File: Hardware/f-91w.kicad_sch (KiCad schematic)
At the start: 1 part, among them U2 LCD-F-91W

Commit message: Update Schematic and Add PIC and BME280 symbols
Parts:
- added C1: 4.7u, Capacitors_SMD:C_0402, symbol C
- added C2, C3: 22p, Capacitors_SMD:C_0402, symbol C
- added P1, P10, P11, P13, P14, P15, P2, P3, P4, P5, P6, P7, P8, P9: CONN_01X01, Connect:1pin, symbol Connector_Generic:Conn_01x01
- added Q1: BC846, Package_TO_SOT_SMD:SOT-23, symbol Transistor_BJT:BC846
- added R1: 10k, Resistors_SMD:R_0402, symbol R
- added R2: 47k, Resistors_SMD:R_0402, symbol Device:R
- added R3: 100, Resistors_SMD:R_0402, symbol Device:R
- U2: symbol LCD-F-91W -> f-91w:LCD-F-91W
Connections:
- net B_ALARM: now also P7.1 (Pin_1)
- net B_LIGHT: now also P5.1 (Pin_1)
- net B_MODE: now also P6.1 (Pin_1)
- net LCD_COM1: now also U2.7
- net LCD_COM2: now also U2.8
- net LCD_COM3: now also U2.9
- net LCD_SEG1: now also U2.1
- net LCD_SEG10: now also U2.13
- net LCD_SEG11: now also U2.14
- net LCD_SEG12: now also U2.15
- net LCD_SEG13: now also U2.16
- net LCD_SEG14: now also U2.17
- net LCD_SEG15: now also U2.18
- net LCD_SEG16: now also U2.19
- net LCD_SEG17: now also U2.20
- net LCD_SEG18: now also U2.21
- net LCD_SEG19: now also U2.22
- net LCD_SEG2: now also U2.2
- net LCD_SEG20: now also U2.23
- net LCD_SEG21: now also U2.24
- net LCD_SEG22: now also U2.25
- net LCD_SEG23: now also U2.26
- net LCD_SEG24: now also U2.27
- net LCD_SEG3: now also U2.3
- net LCD_SEG4: now also U2.4
- net LCD_SEG5: now also U2.5
- net LCD_SEG6: now also U2.6
- net LCD_SEG7: now also U2.10
- net LCD_SEG8: now also U2.11
- net LCD_SEG9: now also U2.12
- net LED_1: now also P11.1 (Pin_1)
- net LED_2: now also R3.2
- net Q-1: now also P1.1 (Pin_1)
- net Q-2: now also P2.1 (Pin_1)
- new net: Q1.1 (B), R2.2
- new net: P10.1 (Pin_1), R3.1
- new net BUZ: P9.1 (Pin_1), Q1.3 (C)
- new net GND: P13.1 (Pin_1), Q1.2 (E)
- new net VCC: P14.1 (Pin_1), P8.1 (Pin_1)

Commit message: Add PIC and BME in schematic
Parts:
- removed C1: 4.7u, Capacitors_SMD:C_0402, symbol C
- removed C2, C3: 22p, Capacitors_SMD:C_0402, symbol C
- removed P1, P2, P3, P4: CONN_01X01, Connect:1pin, symbol Connector_Generic:Conn_01x01
- removed R1: 10k, Resistors_SMD:R_0402, symbol R
- added C? (x2): C, symbol Device:C
- added J?: UART, symbol Connector_Generic:Conn_01x02
- added J?: Programming connector, symbol Connector_Generic:Conn_01x05
- added U?: BME280, symbol f-91w:BME280
- added U?: PIC24FJ128GL306, symbol f-91w:PIC24FJ128GL306
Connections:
- net LED_1 is gone; now on net GND: P11.1 (Pin_1)
- net BUZ: now also R2.1, U?.16 (SEG7)
- net B_ALARM: now also U?.5 (RP26)
- net B_LIGHT: now also U?.35 (RP5)
- net B_MODE: now also U?.34 (RP30)
- net GND: now also C?.2, C?.2, J?.3 (Pin_3), U?.1 (Gnd), U?.7 (Gnd)
- net LCD_COM1: now also U?.62 (COM1)
- net LCD_COM2: now also U?.61 (COM2)
- net LCD_COM3: now also U?.60 (COM3)
- net LCD_SEG1: now also U?.8 (SEG1)
- net LCD_SEG10: now also U?.31 (SEG10)
- net LCD_SEG11: now also U?.32 (SEG11)
- net LCD_SEG12: now also U?.33 (SEG12)
- net LCD_SEG13: now also U?.42 (SEG13)
- net LCD_SEG14: now also U?.43 (SEG14)
- net LCD_SEG15: now also U?.44 (SEG15)
- net LCD_SEG16: now also U?.45 (SEG16)
- net LCD_SEG17: now also U?.46 (SEG17)
- net LCD_SEG18: now also U?.27 (SEG18)
- net LCD_SEG19: now also U?.28 (SEG19)
- net LCD_SEG2: now also U?.11 (SEG2)
- net LCD_SEG21: now also U?.50 (SEG21)
- net LCD_SEG22: now also U?.51 (SEG22)
- net LCD_SEG23: now also U?.52 (SEG23)
- net LCD_SEG24: now also U?.53 (SEG24)
- net LCD_SEG3: now also U?.12 (SEG3)
- net LCD_SEG4: now also U?.13 (SEG4)
- net LCD_SEG5: now also U?.14 (SEG5)
- net LCD_SEG6: now also U?.15 (SEG6)
- net LCD_SEG7: now also U?.16 (SEG7)
- net LCD_SEG8: now also U?.29 (SEG8)
- net LCD_SEG9: now also U?.30 (SEG9)
- net LED_2: now also U?.18 (RP7)
- net VCC: now also C?.1, C?.1, J?.2 (Pin_2), U?.6 (Vdd), U?.8 (Vdd)
- new net MCLR: J?.1 (Pin_1), U?.7 (MCLR)
- new net PGC: J?.1 (Pin_1), J?.5 (Pin_5), U?.17 (RP6)
- new net PGD: J?.2 (Pin_2), J?.4 (Pin_4), U?.18 (RP7)
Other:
- moved on the sheet: P10, P11, P13, P14, P15, P5, P6, P7, P8, P9, Q1, R2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

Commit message: Add temporary symbols to check
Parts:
- added C1, C2, C3, C5, C6: 0.1uf, Capacitor_SMD:C_0402_1005Metric, symbol Device:C
- added C4: C, Capacitor_SMD:C_0402_1005Metric, symbol Device:C
- added C7: 10uf, Capacitor_SMD:C_0402_1005Metric, symbol Device:C
- added C8, C9: 22pF, Capacitor_SMD:C_0402_1005Metric, symbol Device:C
- added P1, P2: CONN_01X01, Connect:1pin, symbol Connector_Generic:Conn_01x01
- added R1, R4: R, Resistor_SMD:R_0402_1005Metric, symbol Device:R
- added Y1: 32.768 kHz, Crystal:Crystal_AT310_D3.0mm_L10.0mm_Horizontal, symbol Device:Crystal
- C10, C11: renamed from C?; value C -> 0.1uF; footprint (none) -> Capacitor_SMD:C_0402_1005Metric
- J1: renamed from J?; footprint (none) -> Connector_PinHeader_1.00mm:PinHeader_1x02_P1.00mm_Vertical
- J2: renamed from J?; footprint (none) -> Connector_PinHeader_1.00mm:PinHeader_1x05_P1.00mm_Vertical
- U1: renamed from U?; footprint (none) -> Package_DFN_QFN:Microchip_DRQFN-64-1EP_7x7mm_P0.65mm_EP4.1x4.1mm
- U3: renamed from U?; footprint (none) -> Package_LGA:LGA-8_3x5mm_P1.25mm
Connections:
- net GND: now also U1.20 (AVss), U1.25 (Vss), U1.41 (Vss), U1.9 (Vss), C1.2, C2.2, C3.2, C4.2, C5.2, C6.2, C7.2, C8.1, C9.2
- net LCD_SEG20: now also U1.49 (SEG20)
- net MCLR: no longer U1.7 (MCLR)
- net VCC: now also U1.10 (Vdd), U1.19 (AVdd), U1.26 (Vdd), U1.38 (Vdd), C2.1, C3.1, C4.1, C5.1, C6.1, R1.2
- net CSB: now reaches U3.2 (CSB)
- net CSB: now also U1.55 (RD7)
- net SDI: now reaches U3.3 (SDI)
- net SDI: now also U1.54 (RD6)
- net SCK: now reaches U3.4 (SCK)
- net SCK: now also U1.23 (RP15)
- net SDO: now reaches U3.5 (SDO)
- net SDO: now also U1.4 (SEG0)
- net SOSCI: now reaches U1.47 (SOSCI)
- net SOSCI: now also C9.1, Y1.2
- net SOSCO: now reaches U1.48 (SOSO)
- net SOSCO: now also C8.2, Y1.1
- net VCAP: now reaches U1.56 (Vap)
- net VCAP: now also C7.1
- new net: C1.1, P2.1 (Pin_1)
- new net: R4.2, U1.7 (MCLR)
- new net: P1.1 (Pin_1), R1.1, R4.1
- no-connect marks 0 -> 2
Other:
- moved on the sheet: P13, P14, P8

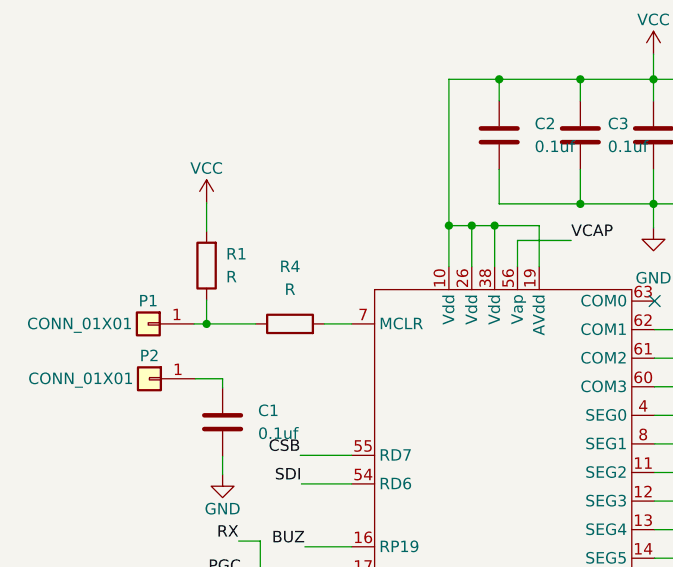
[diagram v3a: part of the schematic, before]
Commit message: Add BME280 footprint
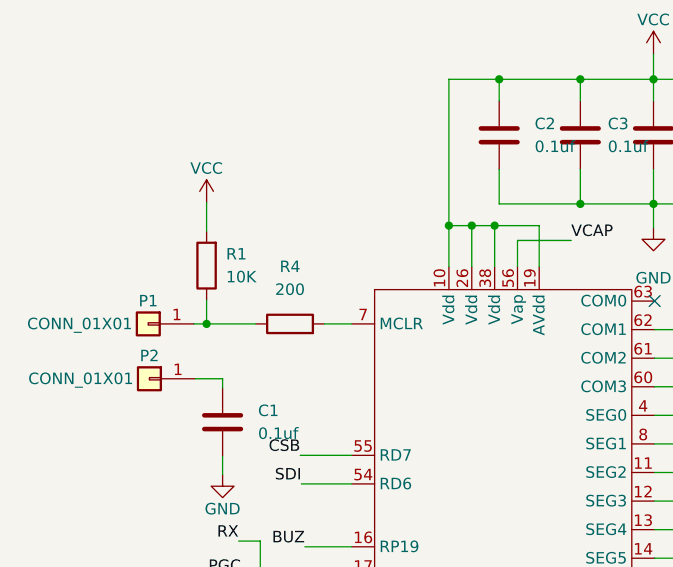
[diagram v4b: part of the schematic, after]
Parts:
- R1: value R -> 10K
- R4: value R -> 200
- U1: footprint Package_DFN_QFN:Microchip_DRQFN-64-1EP_7x7mm_P0.65mm_EP4.1x4.1mm -> Package_DFN_QFN:QFN-64-1EP_9x9mm_P0.5mm_EP7.5x7.5mm
- U3: footprint Package_LGA:LGA-8_3x5mm_P1.25mm -> Package_LGA:Bosch_LGA-8_2.5x2.5mm_P0.65mm_ClockwisePinNumbering
- Y1: footprint Crystal:Crystal_AT310_D3.0mm_L10.0mm_Horizontal -> Crystal:Crystal_SMD_EuroQuartz_EQ161-2Pin_3.2x1.5mm
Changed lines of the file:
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@@
     (property "Reference" "U3" (id 0) (at 243.459 85.979 0))
     (property "Value" "BME280" (id 1) (at 243.459 88.519 0))
-    (property "Footprint" "Package_LGA:LGA-8_3x5mm_P1.25mm" (id 2) (at 239.522 93.345 0)
+    (property "Footprint" "Package_LGA:Bosch_LGA-8_2.5x2.5mm_P0.65mm_ClockwisePinNumbering" (id 2) (at 239.522 93.345 0)
       (effects (font (size 1.27 1.27)) hide)
     )
@@
       (effects (font (size 1.27 1.27)) (justify left))
     )
-    (property "Footprint" "Package_DFN_QFN:Microchip_DRQFN-64-1EP_7x7mm_P0.65mm_EP4.1x4.1mm" (id 2) (at 57.15 99.06 0)
+    (property "Footprint" "Package_DFN_QFN:QFN-64-1EP_9x9mm_P0.5mm_EP7.5x7.5mm" (id 2) (at 57.15 99.06 0)
       (effects (font (size 1.27 1.27)) hide)
     )
@@
     (property "Reference" "Y1" (id 0) (at 223.52 139.7 0))
     (property "Value" "32.768 kHz" (id 1) (at 223.52 142.24 0))
-    (property "Footprint" "Crystal:Crystal_AT310_D3.0mm_L10.0mm_Horizontal" (id 2) (at 223.52 147.193 0)
+    (property "Footprint" "Crystal:Crystal_SMD_EuroQuartz_EQ161-2Pin_3.2x1.5mm" (id 2) (at 223.52 147.193 0)
       (effects (font (size 1.27 1.27)) hide)
     )
@@
     (in_bom yes) (on_board yes) (fields_autoplaced)
     (property "Reference" "R4" (id 0) (at 43.942 91.44 90))
-    (property "Value" "R" (id 1) (at 43.942 93.98 90))
+    (property "Value" "200" (id 1) (at 43.942 93.98 90))
     (property "Footprint" "Resistor_SMD:R_0402_1005Metric" (id 2) (at 43.942 99.568 90)
       (effects (font (size 1.27 1.27)) hide)
@@
       (effects (font (size 1.27 1.27)) (justify right))
     )
-    (property "Value" "R" (id 1) (at 36.83 92.5829 0)
+    (property "Value" "10K" (id 1) (at 36.83 92.5829 0)
       (effects (font (size 1.27 1.27)) (justify right))
     )
@@
     )
     (path "/e46c5713-29f9-48c8-944d-bc0b917efa29"
-      (reference "R1") (unit 1) (value "R") (footprint "Resistor_SMD:R_0402_1005Metric")
+      (reference "R1") (unit 1) (value "10K") (footprint "Resistor_SMD:R_0402_1005Metric")
     )
     (path "/00000000-0000-0000-0000-000056edfaa4"
@@
     )
     (path "/bc715fd3-2d9e-4872-9def-1ba7182937fb"
-      (reference "R4") (unit 1) (value "R") (footprint "Resistor_SMD:R_0402_1005Metric")
+      (reference "R4") (unit 1) (value "200") (footprint "Resistor_SMD:R_0402_1005Metric")
     )
     (path "/7f944b03-2f3e-414f-bfc7-50e5068b4e87"
-      (reference "U1") (unit 1) (value "PIC24FJ128GL306") (footprint "Package_DFN_QFN:Microchip_DRQFN-64-1EP_7x7mm_P0.65mm_EP4.1x4.1mm")
+      (reference "U1") (unit 1) (value "PIC24FJ128GL306") (footprint "Package_DFN_QFN:QFN-64-1EP_9x9mm_P0.5mm_EP7.5x7.5mm")
     )
     (path "/00000000-0000-0000-0000-000056e8a641"
@@
     )
     (path "/36369fd3-9842-43d9-8256-2baed409a037"
-      (reference "U3") (unit 1) (value "BME280") (footprint "Package_LGA:LGA-8_3x5mm_P1.25mm")
+      (reference "U3") (unit 1) (value "BME280") (footprint "Package_LGA:Bosch_LGA-8_2.5x2.5mm_P0.65mm_ClockwisePinNumbering")
     )
     (path "/90ea2159-7d74-4a6c-93bb-56e11d973677"
-      (reference "Y1") (unit 1) (value "32.768 kHz") (footprint "Crystal:Crystal_AT310_D3.0mm_L10.0mm_Horizontal")
-    )
-  )
+      (reference "Y1") (unit 1) (value "32.768 kHz") (footprint "Crystal:Crystal_SMD_EuroQuartz_EQ161-2Pin_3.2x1.5mm")
+    )
+  )

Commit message: Update BOM, schematic and footprint.
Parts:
- C1, C10, C11, C2, C3, C5, C6, C8, C9: footprint Capacitor_SMD:C_0402_1005Metric -> Capacitor_SMD:C_0201_0603Metric_Pad0.64x0.40mm_HandSolder
- C4: value C -> 0.1uf; footprint Capacitor_SMD:C_0402_1005Metric -> Capacitor_SMD:C_0201_0603Metric_Pad0.64x0.40mm_HandSolder
- C7: footprint Capacitor_SMD:C_0402_1005Metric -> Capacitor_SMD:C_0402_1005Metric_Pad0.74x0.62mm_HandSolder
- Y1: value 32.768 kHz -> ABS07-32.768KHZ-T; footprint Crystal:Crystal_SMD_EuroQuartz_EQ161-2Pin_3.2x1.5mm -> Crystal:Crystal_SMD_EuroQuartz_EQ161-2Pin_3.2x1.5mm_HandSoldering
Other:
- moved on the sheet: C1, C10, C11, C2, C3, C4, C5, C6, C7, J1, J2, P1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
